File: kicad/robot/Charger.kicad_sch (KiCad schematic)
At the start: 32 parts, among them U13 MAX77976EFD+

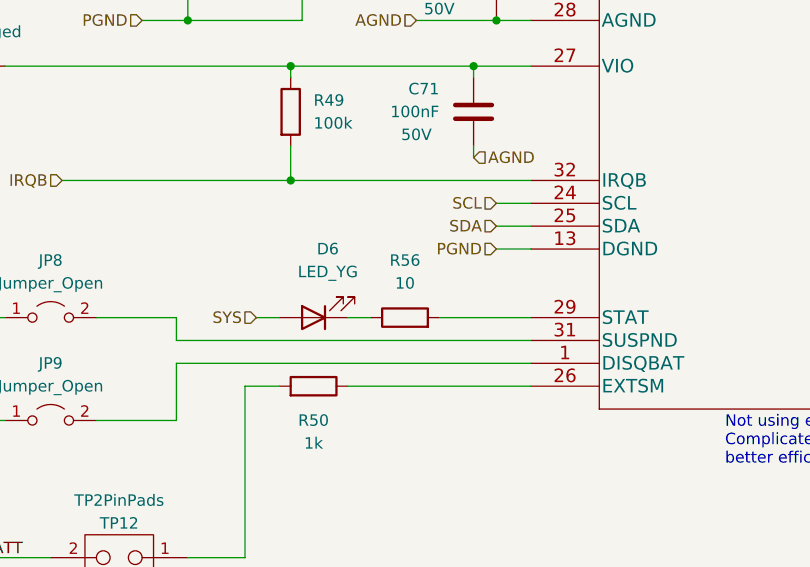
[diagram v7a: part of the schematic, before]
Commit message: Update resistor on R56 to reduce current in LED
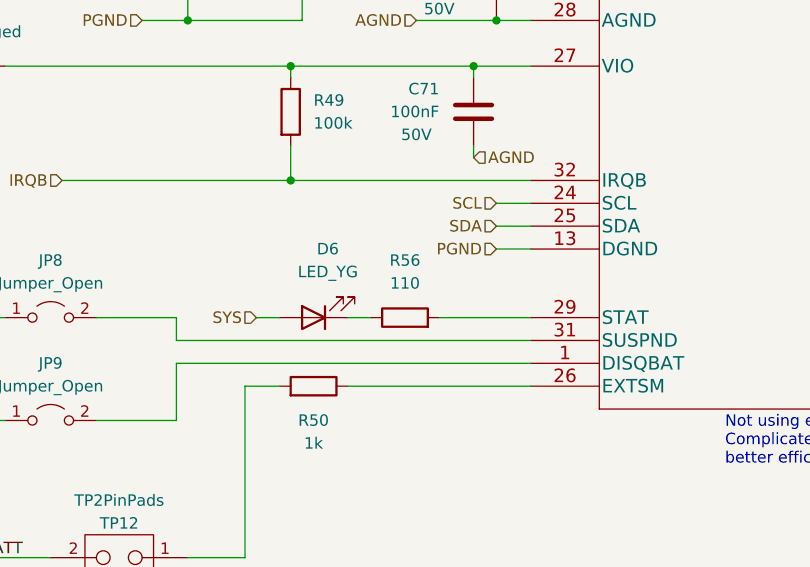
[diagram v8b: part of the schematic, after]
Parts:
- R56: value 10 -> 110
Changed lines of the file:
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@@
     (in_bom yes) (on_board yes) (fields_autoplaced)
     (property "Reference" "R56" (id 0) (at 82.55 130.81 90))
-    (property "Value" "10" (id 1) (at 82.55 133.35 90))
+    (property "Value" "110" (id 1) (at 82.55 133.35 90))
     (property "Footprint" "Resistor_SMD:R_0603_1608Metric" (id 2) (at 82.55 138.938 90)
       (effects (font (size 1.27 1.27)) hide)
@@
       (effects (font (size 1.27 1.27)) hide)
     )
+    (property "Description" "1/16 W" (id 4) (at 82.55 137.16 0)
+      (effects (font (size 1.27 1.27)) hide)
+    )
